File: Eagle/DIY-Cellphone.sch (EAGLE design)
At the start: 67 parts, among them IC1 MEGA1284, J1 ISP, U1 MCP73831, U7 M10_HDWITHOUT_EXCLUSION, X1 BU-SMA-V, X3 CCM03-3002 R102

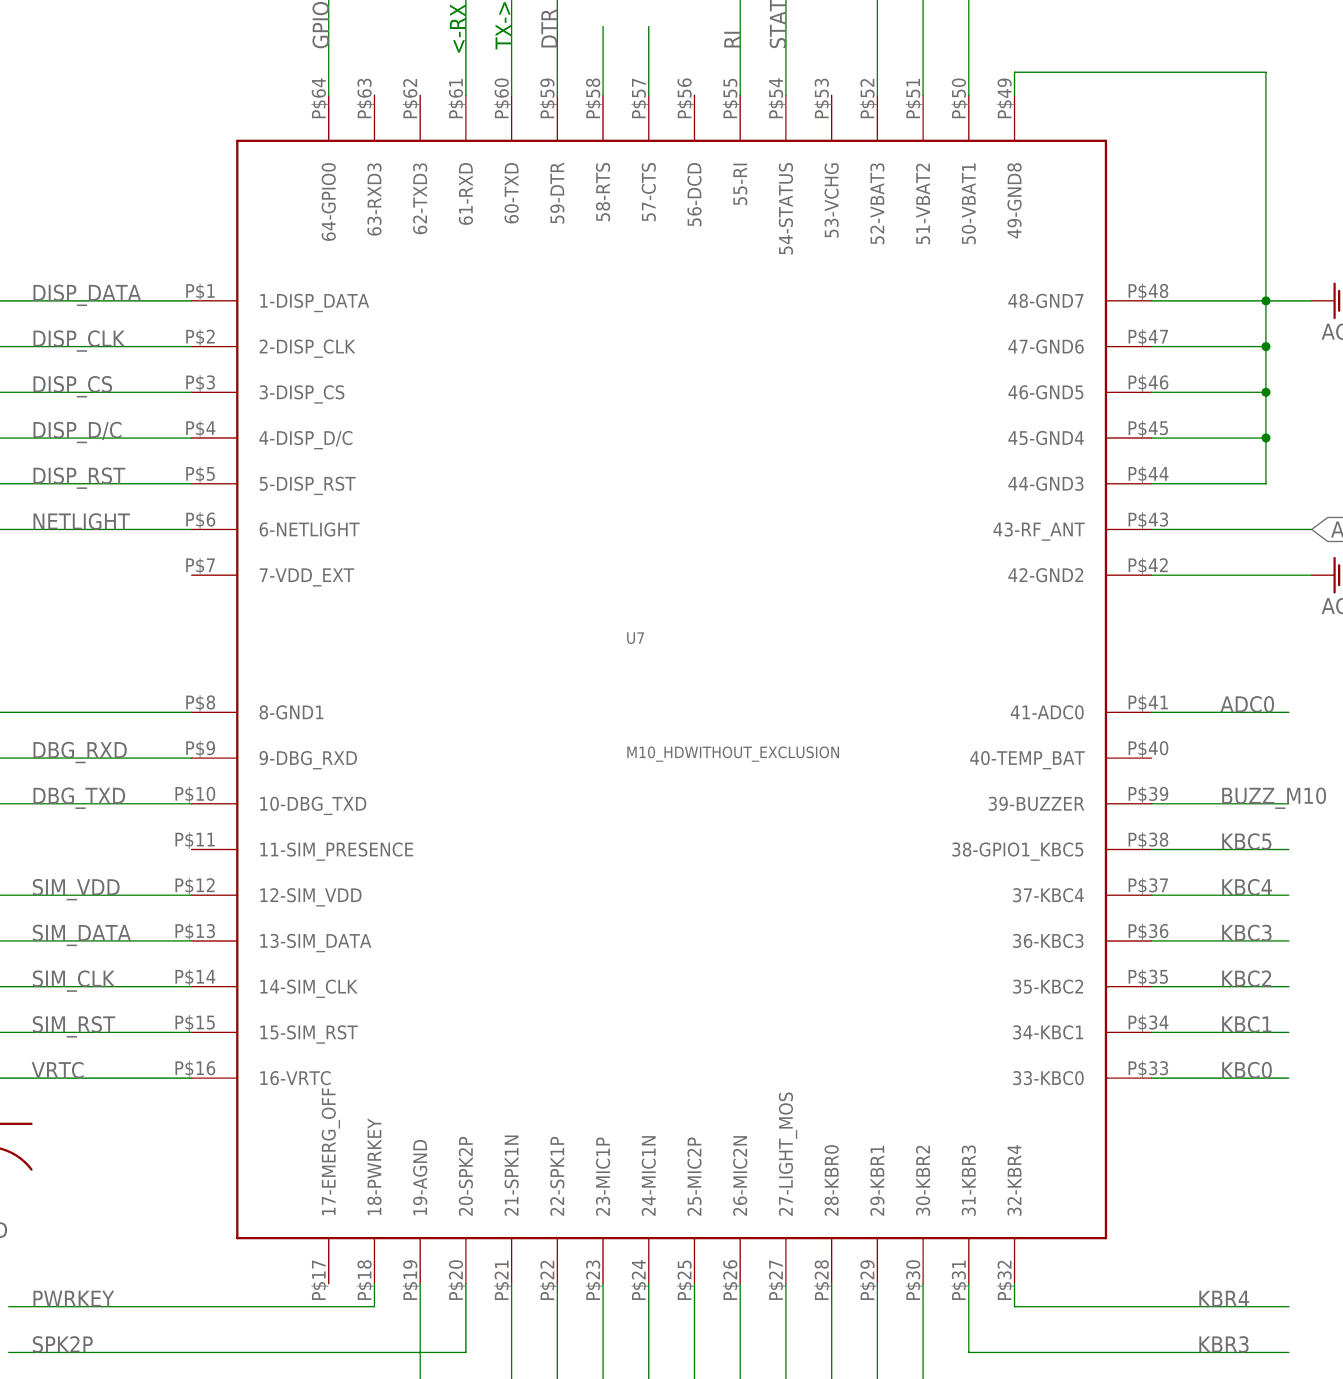
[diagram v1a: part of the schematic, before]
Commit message: Create UC15 footprint; replace M10 w/ UC15.
Warning: this board won’t work! Note that many of the traces on the
board now overlap the new pads on the UC15 (that aren’t on the M10).
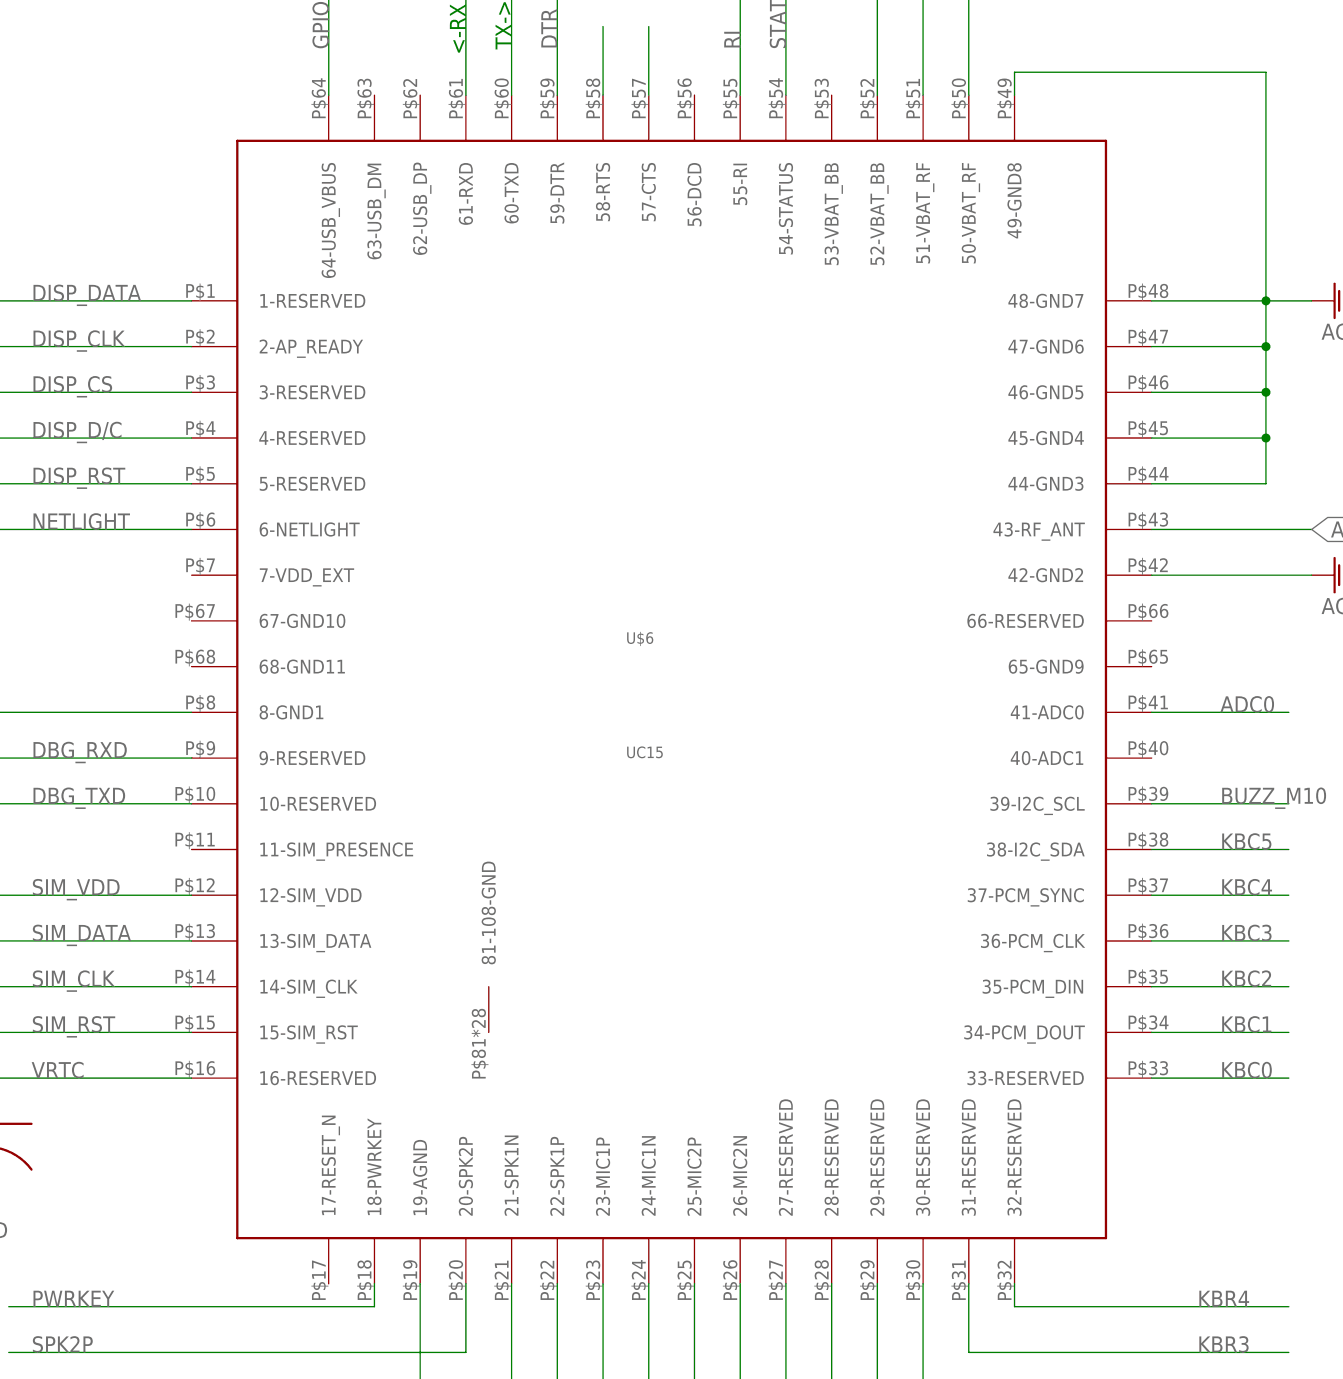
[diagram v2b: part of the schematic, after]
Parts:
- removed U7: M10_HDWITHOUT_EXCLUSION, GSM:M10_HDWITHOUT_EXCLUSION
- added U$6: UC15, cellphone:UC15
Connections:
- net ADC0: now also U$6.41-ADC0; no longer U7.41-ADC0
- net ANT: now also U$6.43-RF_ANT; no longer U7.43-RF_ANT
- net BUZZ_M10: now also U$6.39-I2C_SCL; no longer U7.39-BUZZER
- net DBG_RXD: now also U$6.9-RESERVED; no longer U7.9-DBG_RXD
- net DBG_TXD: now also U$6.10-RESERVED; no longer U7.10-DBG_TXD
- net DISP_CLK: now also U$6.2-AP_READY; no longer U7.2-DISP_CLK
- net DISP_CS: now also U$6.3-RESERVED; no longer U7.3-DISP_CS
- net DISP_D/C: now also U$6.4-RESERVED; no longer U7.4-DISP_D/C
- net DISP_DATA: now also U$6.1-RESERVED; no longer U7.1-DISP_DATA
- net DISP_RST: now also U$6.5-RESERVED; no longer U7.5-DISP_RST
- net DTR: now also U$6.59-DTR; no longer U7.59-DTR
- net GND: now also U$6.19-AGND, U$6.42-GND2, U$6.44-GND3, U$6.45-GND4, U$6.46-GND5, U$6.47-GND6, U$6.48-GND7, U$6.49-GND8, U$6.8-GND1; no longer U7.19-AGND, U7.42-GND2, U7.44-GND3, U7.45-GND4, U7.46-GND5, U7.47-GND6, U7.48-GND7, U7.49-GND8, U7.8-GND1
- net GPIO0: now also U$6.64-USB_VBUS; no longer U7.64-GPIO0
- net KBC0: now also U$6.33-RESERVED; no longer U7.33-KBC0
- net KBC1: now also U$6.34-PCM_DOUT; no longer U7.34-KBC1
- net KBC2: now also U$6.35-PCM_DIN; no longer U7.35-KBC2
- net KBC3: now also U$6.36-PCM_CLK; no longer U7.36-KBC3
- net KBC4: now also U$6.37-PCM_SYNC; no longer U7.37-KBC4
- net KBC5: now also U$6.38-I2C_SDA; no longer U7.38-GPIO1_KBC5
- net KBR0: now also U$6.28-RESERVED; no longer U7.28-KBR0
- net KBR1: now also U$6.29-RESERVED; no longer U7.29-KBR1
- net KBR2: now also U$6.30-RESERVED; no longer U7.30-KBR2
- net KBR3: now also U$6.31-RESERVED; no longer U7.31-KBR3
- net KBR4: now also U$6.32-RESERVED; no longer U7.32-KBR4
- net LIGHT_MOS: now also U$6.27-RESERVED; no longer U7.27-LIGHT_MOS
- net MIC1N: now also U$6.24-MIC1N; no longer U7.24-MIC1N
- net MIC1P: now also U$6.23-MIC1P; no longer U7.23-MIC1P
- net MIC2N: now also U$6.26-MIC2N; no longer U7.26-MIC2N
- net MIC2P: now also U$6.25-MIC2P; no longer U7.25-MIC2P
- net N$1: now also U$6.57-CTS; no longer U7.57-CTS
- net N$43: now also U$6.58-RTS; no longer U7.58-RTS
- net NETLIGHT: now also U$6.6-NETLIGHT; no longer U7.6-NETLIGHT
- net PWRKEY: now also U$6.18-PWRKEY; no longer U7.18-PWRKEY
- net RI: now also U$6.55-RI; no longer U7.55-RI
- net RXD1: now also U$6.60-TXD; no longer U7.60-TXD
- net SIM_CLK: now also U$6.14-SIM_CLK; no longer U7.14-SIM_CLK
- net SIM_DATA: now also U$6.13-SIM_DATA; no longer U7.13-SIM_DATA
- net SIM_RST: now also U$6.15-SIM_RST; no longer U7.15-SIM_RST
- net SIM_VDD: now also U$6.12-SIM_VDD; no longer U7.12-SIM_VDD
- net SPK1N: now also U$6.21-SPK1N; no longer U7.21-SPK1N
- net SPK1P: now also U$6.22-SPK1P; no longer U7.22-SPK1P
- net SPK2P: now also U$6.20-SPK2P; no longer U7.20-SPK2P
- net STATUS: now also U$6.54-STATUS; no longer U7.54-STATUS
- net TXD1: now also U$6.61-RXD; no longer U7.61-RXD
- net VCC: now also U$6.50-VBAT_RF, U$6.51-VBAT_RF, U$6.52-VBAT_BB; no longer U7.50-VBAT1, U7.51-VBAT2, U7.52-VBAT3
- net VRTC: now also U$6.16-RESERVED; no longer U7.16-VRTC

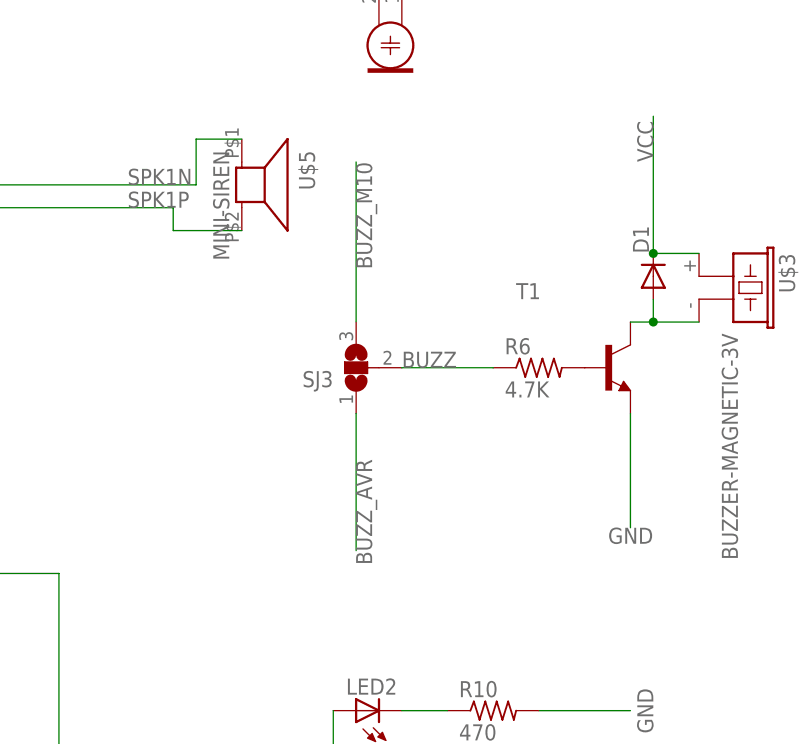
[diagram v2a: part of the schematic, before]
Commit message: Connect buzzer directly to microcontroller.
Remove solder jumper that allows it to go to the Quectel module, since
the UC15 drops the buzzer pin.
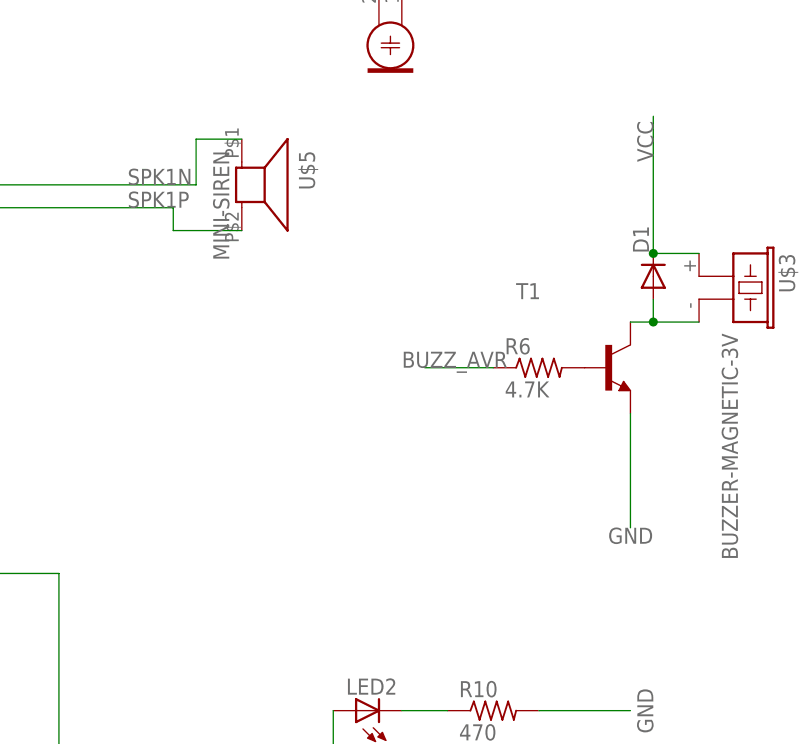
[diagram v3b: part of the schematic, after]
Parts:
- removed SJ3: (no value), jumper:SJ2W
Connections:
- removed net BUZZ: R6.1, SJ3.2
- net BUZZ_AVR: now also R6.1; no longer SJ3.1
- net BUZZ_M10: no longer SJ3.3
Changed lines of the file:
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@@
 <part name="R10" library="cellphone-rcl" deviceset="R-US_" device="R1206" value="470"/>
 <part name="U$2" library="cellphone" deviceset="HCMS-[23]97X" device=""/>
-<part name="SJ3" library="jumper" deviceset="SJ2W" device=""/>
 <part name="JP2" library="pinhead" deviceset="PINHD-1X4" device=""/>
 <part name="U$6" library="cellphone" deviceset="UC15" device=""/>
@@
 <instance part="R10" gate="G$1" x="177.8" y="175.26"/>
 <instance part="U$2" gate="G$1" x="58.42" y="246.38" rot="R270"/>
-<instance part="SJ3" gate="G$1" x="162.56" y="213.36" rot="R180"/>
 <instance part="JP2" gate="A" x="38.1" y="81.28"/>
 <instance part="U$6" gate="G$1" x="147.32" y="91.44"/>
@@
 </segment>
 </net>
-<net name="BUZZ" class="0">
-<segment>
-<pinref part="R6" gate="G$1" pin="1"/>
-<wire x1="177.8" y1="213.36" x2="167.64" y2="213.36" width="0.1524" layer="91"/>
-<label x="167.64" y="213.36" size="1.778" layer="95"/>
-<pinref part="SJ3" gate="G$1" pin="2"/>
-</segment>
-</net>
 <net name="KBC5" class="0">
 <segment>
@@
 </segment>
 <segment>
-<pinref part="SJ3" gate="G$1" pin="1"/>
-<wire x1="162.56" y1="208.28" x2="162.56" y2="193.04" width="0.1524" layer="91"/>
-<label x="162.56" y="203.2" size="1.778" layer="95" rot="R270"/>
+<pinref part="R6" gate="G$1" pin="1"/>
+<wire x1="177.8" y1="213.36" x2="170.18" y2="213.36" width="0.1524" layer="91"/>
+<label x="167.64" y="213.36" size="1.778" layer="95"/>
 </segment>
 </net>
@@
 <net name="BUZZ_M10" class="0">
 <segment>
-<pinref part="SJ3" gate="G$1" pin="3"/>
-<wire x1="162.56" y1="218.44" x2="162.56" y2="236.22" width="0.1524" layer="91"/>
-<label x="162.56" y="236.22" size="1.778" layer="95" rot="R270"/>
-</segment>
-<segment>
 <wire x1="215.9" y1="68.58" x2="200.66" y2="68.58" width="0.1524" layer="91"/>
